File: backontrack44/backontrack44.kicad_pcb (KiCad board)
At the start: 2 copper layers, 151.1 x 95 mm, 98 parts, among them J1 AudioJack4, J2 OLED, SW1-1 choc_SW_HS, SW1-2 choc_SW_HS, SW1-3 choc_SW_HS, SW1-4 choc_SW_HS, SW1-5 choc_SW_HS, SW1-6 choc_SW_HS, SW2-1 choc_SW_HS, SW2-2 choc_SW_HS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

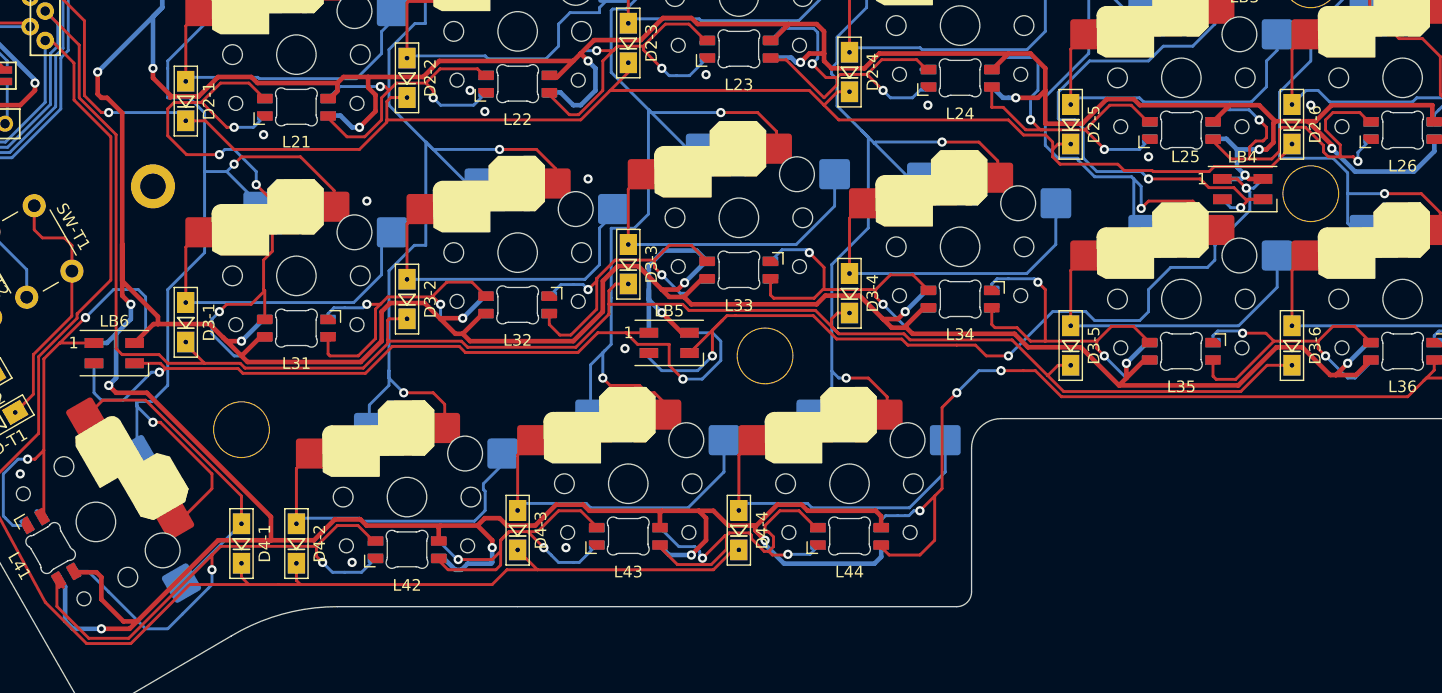
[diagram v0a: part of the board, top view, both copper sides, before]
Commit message: simplified some connections
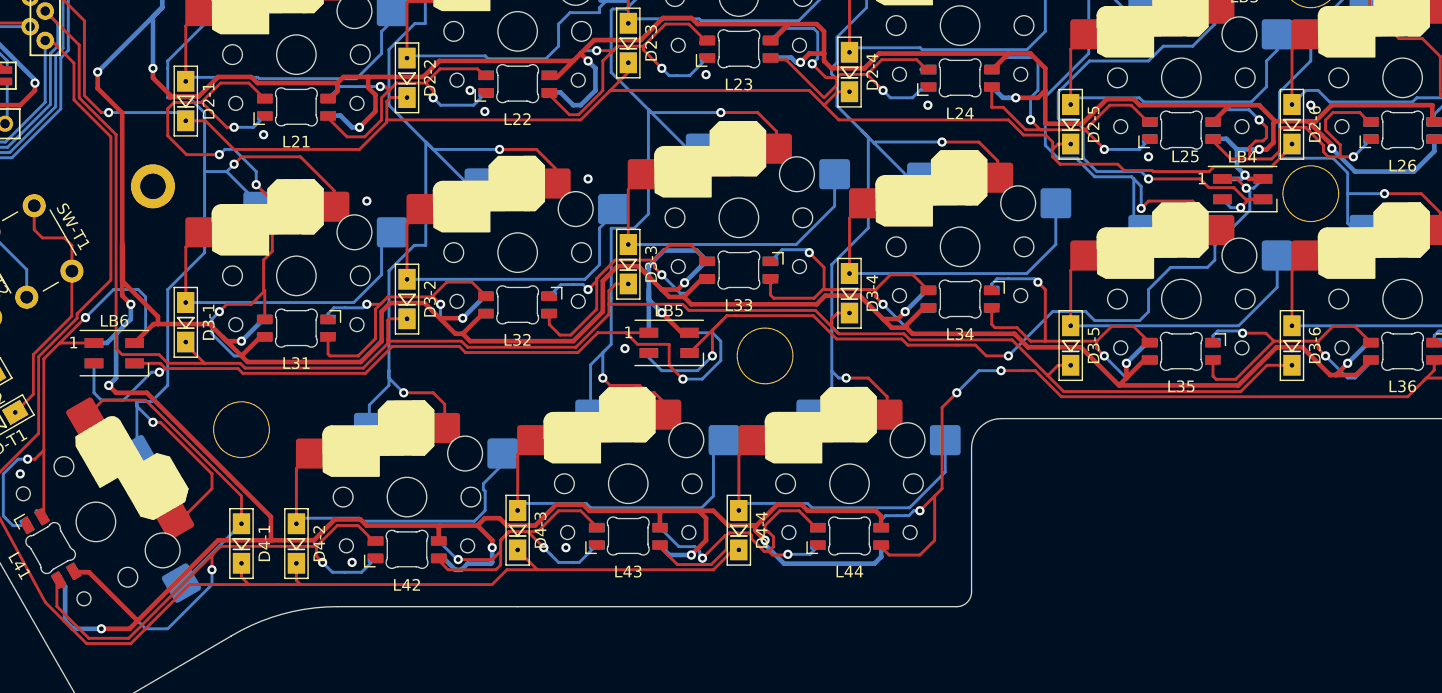
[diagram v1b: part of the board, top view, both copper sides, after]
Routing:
- net VCC: track 862.6 -> 861.1 mm
- net Net-(L25-Pad2): track 36.9 -> 36.1 mm
- net Net-(D4-3-Pad2): track 28.8 -> 29.5 mm

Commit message: added logo
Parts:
- added JLCJLCJLCJLC: production label, Footprints:production label, F.Cu at (51.4, 47.0)
- added esc: Logo, Footprints:Logo, F.Cu at (64.7, 52.3)
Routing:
- net Net-(L24-Pad2): track 35.5 -> 34.9 mm

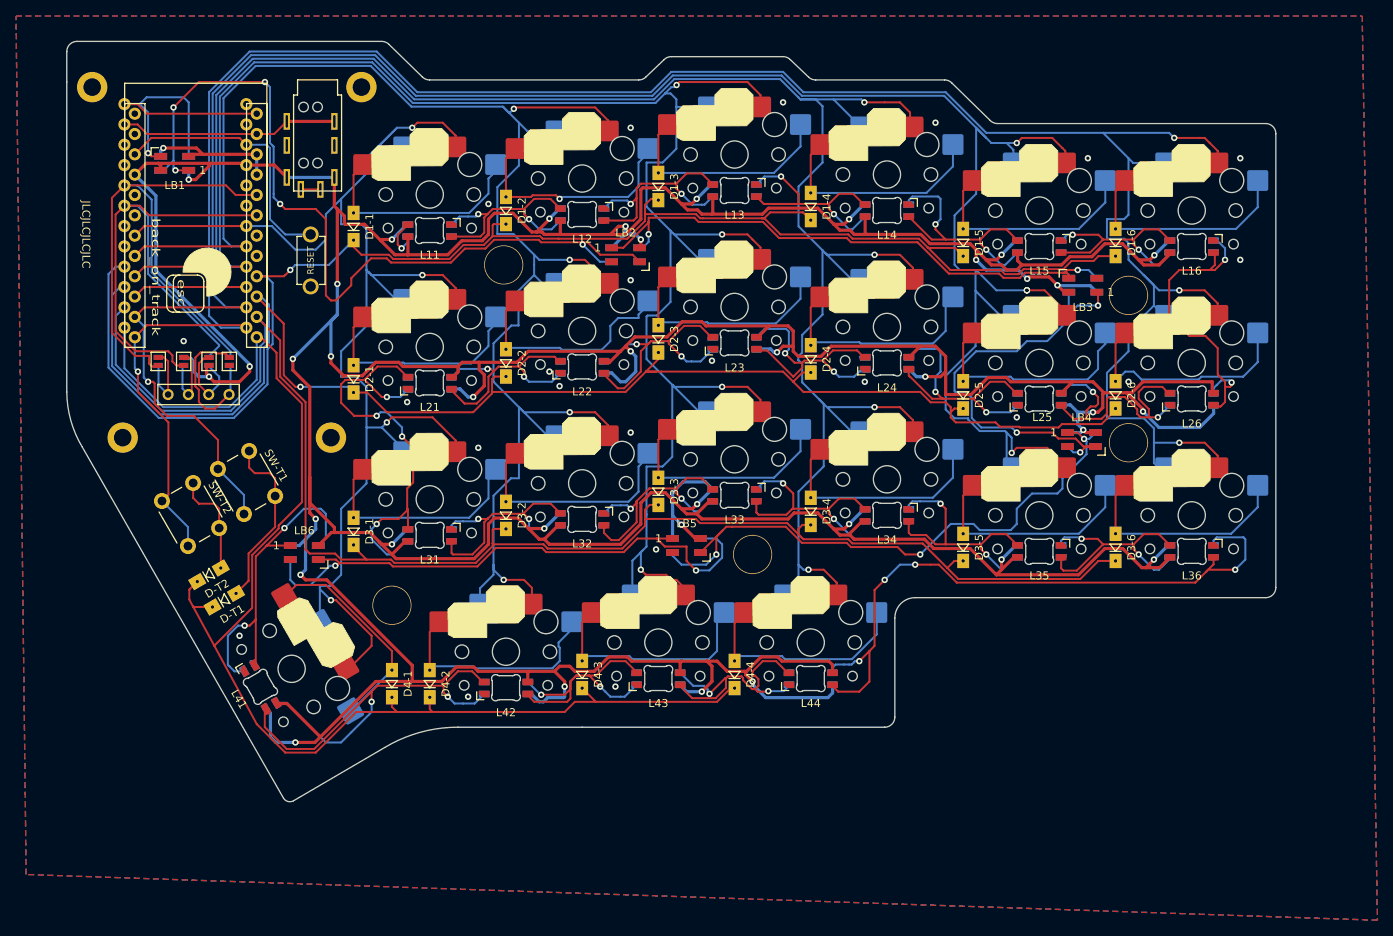
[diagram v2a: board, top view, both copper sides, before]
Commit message: fixed most warnings
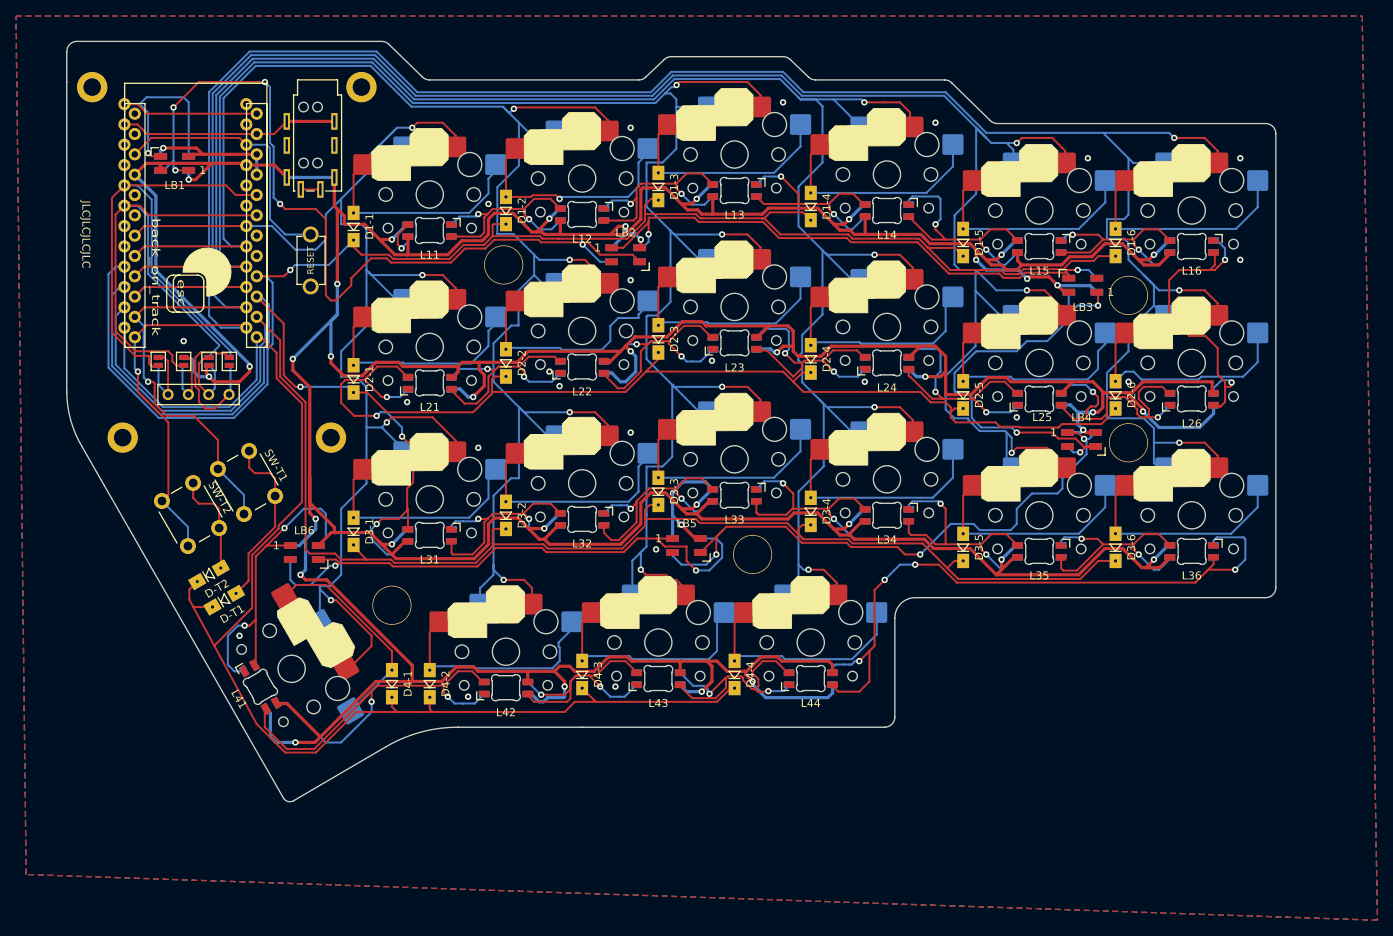
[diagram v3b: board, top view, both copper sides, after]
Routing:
- net GND: track 25.7 -> 22.2 mm
- net VCC: track 861.1 -> 859.6 mm
- net row2: track 182.2 -> 180.9 mm
- net Net-(L41-Pad2): track 61.3 -> 60.5 mm
- net col5: track 284.6 -> 283.9 mm, vias 5 -> 4
- net Net-(J2-Pad3): track 10.5 -> 9.85 mm
- net col1: track 177.9 -> 177.3 mm
